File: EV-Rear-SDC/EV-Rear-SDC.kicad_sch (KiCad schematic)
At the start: 74 parts, among them IC2 SCH16T-K01-10, J1 JST-XA, J2 B10B-XASK-1__LF__SN_, J3 Conn_01x14, J4 Conn_01x03, J5 Conn_01x14, J6 JST-XA, K1 Relay_SPDT_G6RN, Q1 BSS205N, Q10 BSS205N, Q11 BSS205N, Q2 BSS205N, Q3 BSS205N, Q4 BSS205N, Q5 BSS205N, Q6 BSS205N, Q7 BSS205N, Q8 BSS205N, Q9 BSS205N, U1 TXE8116DGSR, U2 MAX3390EEUD_T

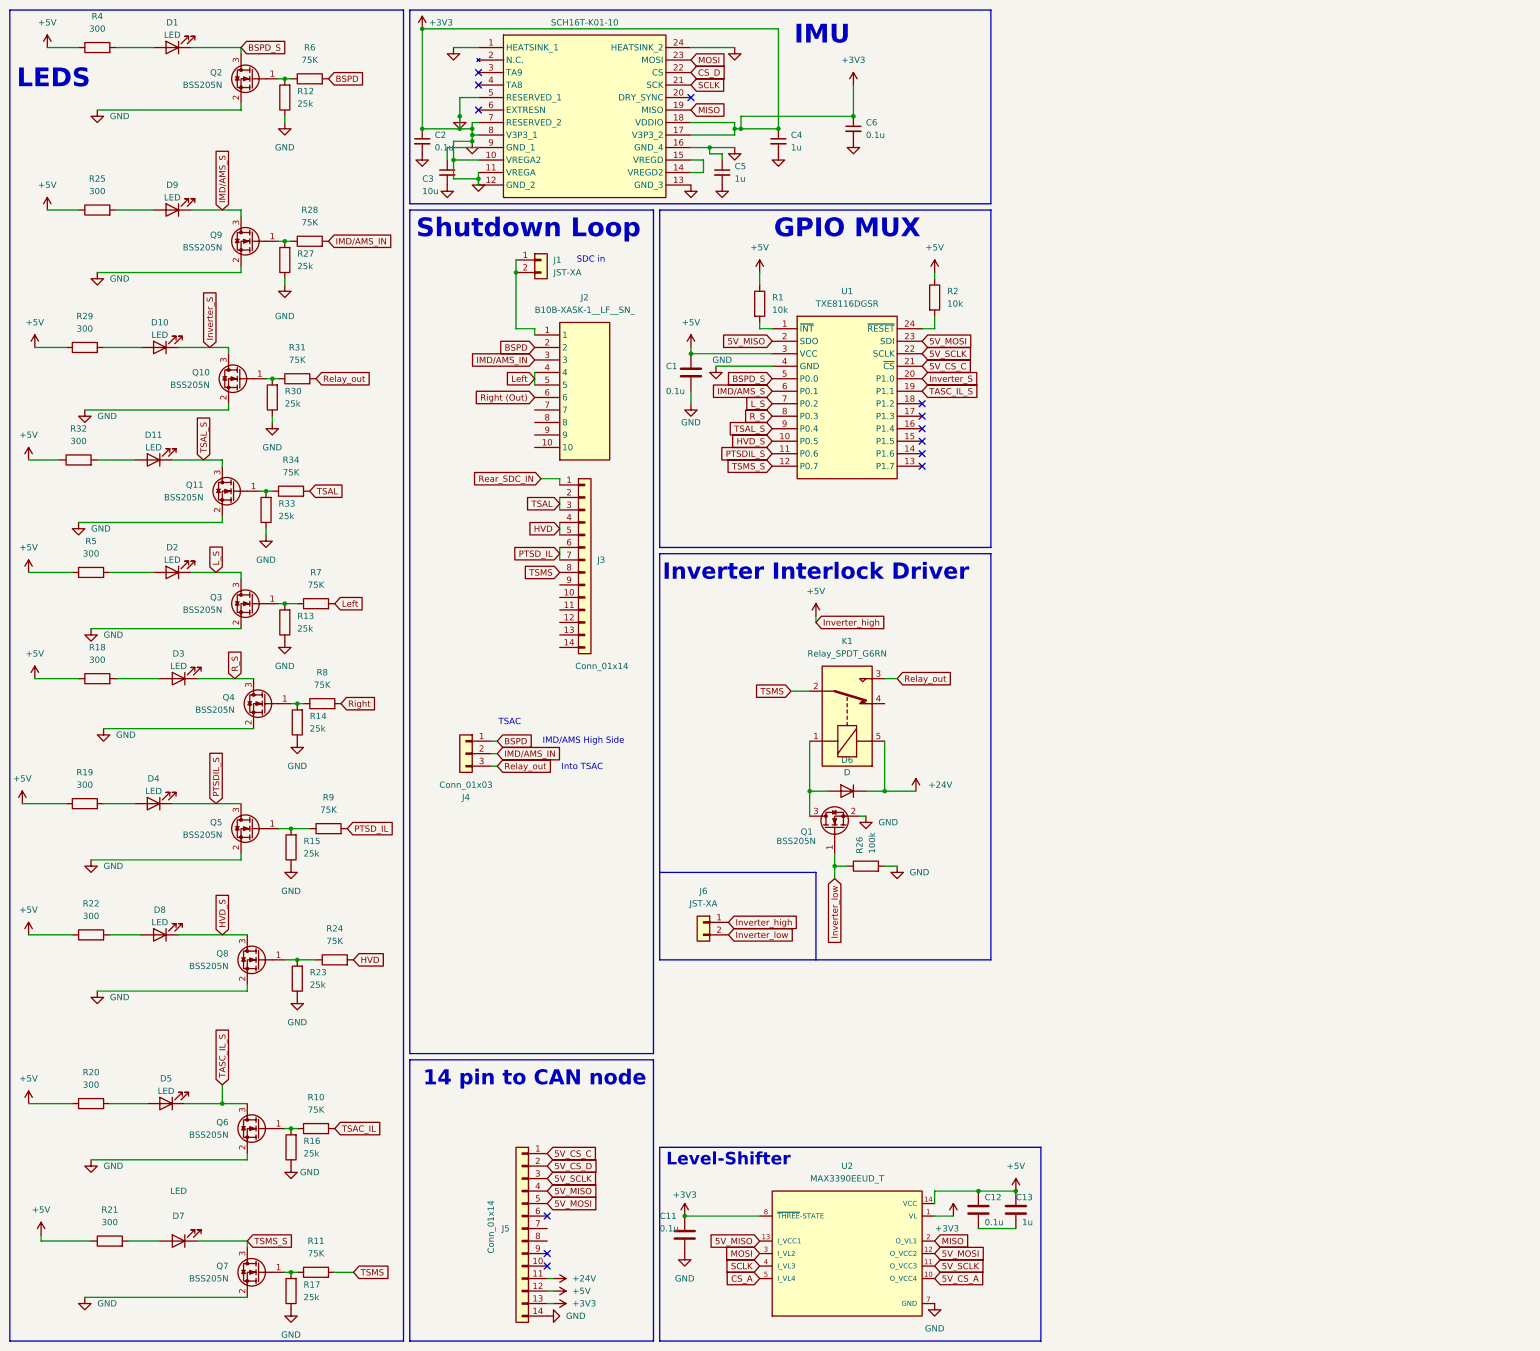
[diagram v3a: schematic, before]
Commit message: Moved Mosfet to avoid EMI error
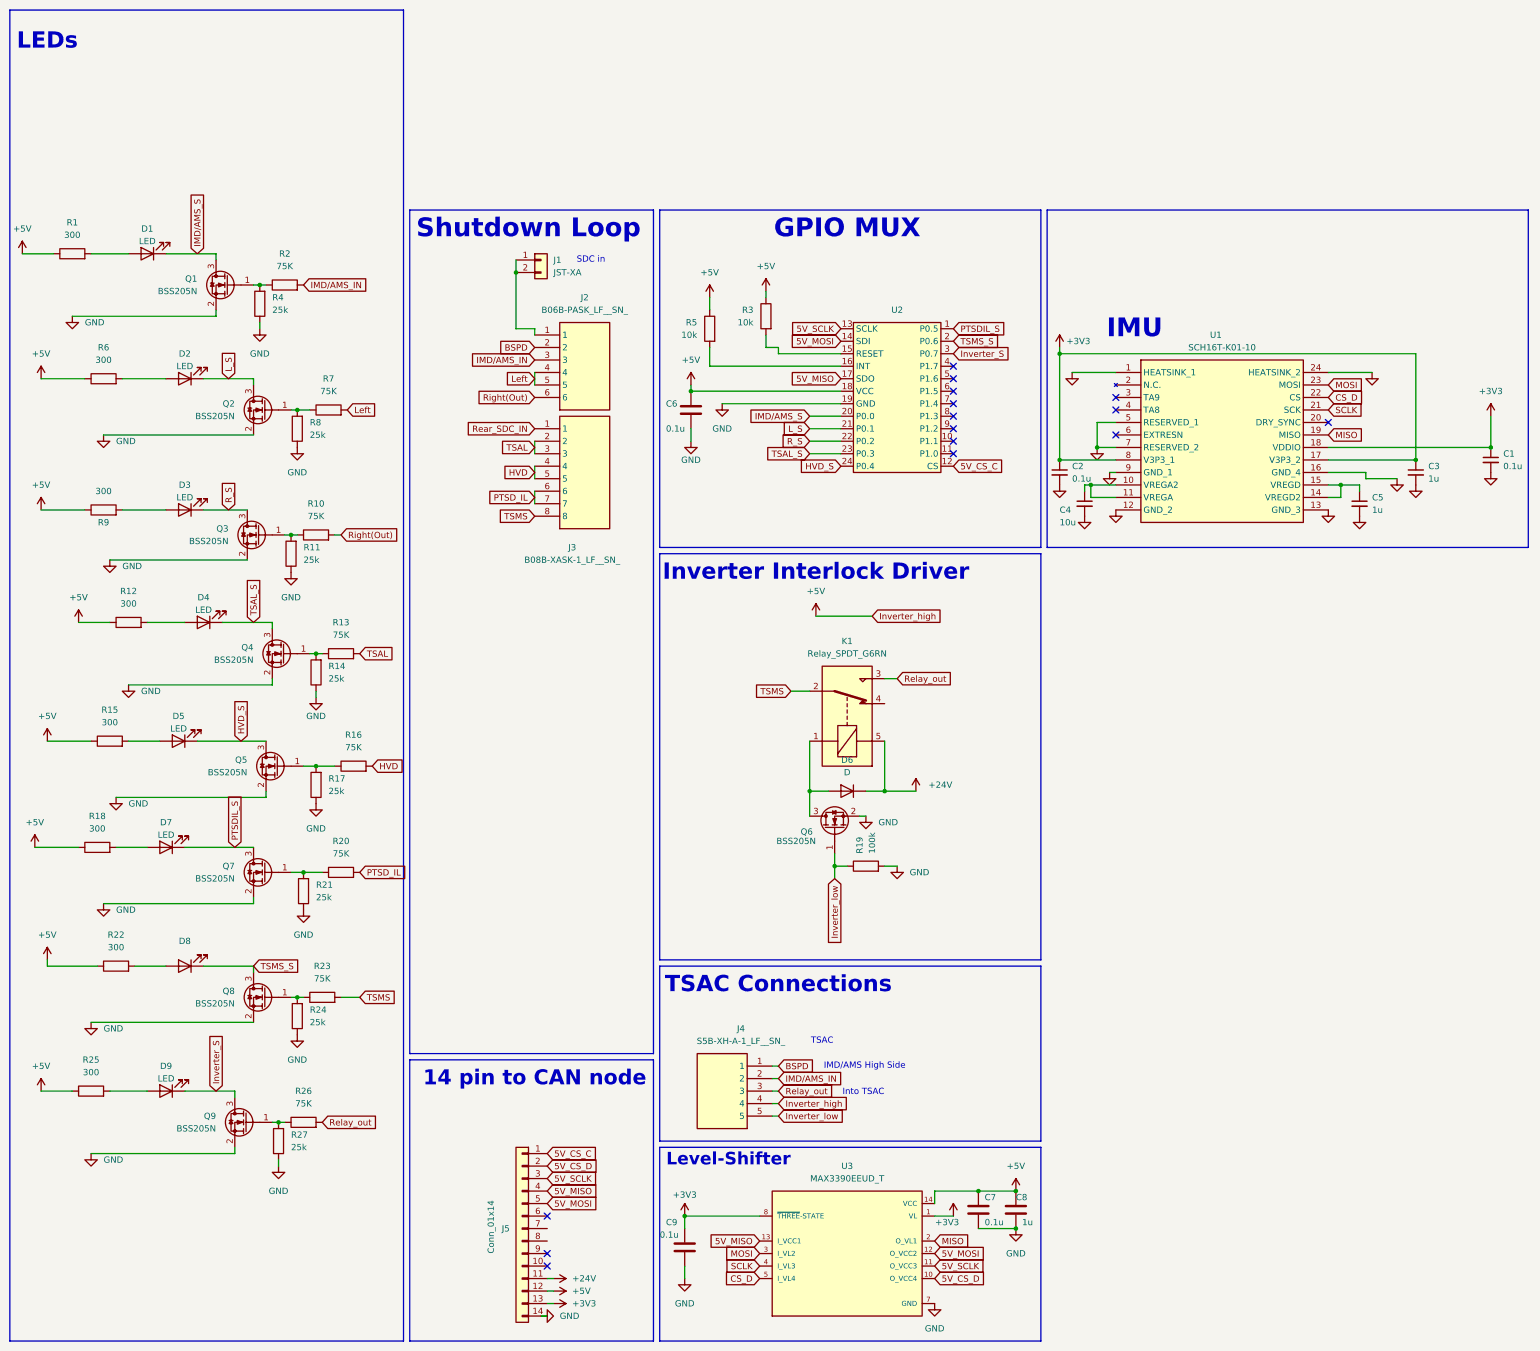
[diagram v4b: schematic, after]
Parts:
- removed C1: 0.1u, Capacitor_SMD:C_0603_1608Metric, symbol Device:C
- removed C6: 0.1u, Capacitor_SMD:C_0603_1608Metric, symbol Device:C_Small
- removed D1, D5: LED, LED_SMD:LED_0603_1608Metric, symbol Device:LED
- removed IC2: SCH16T-K01-10, Custom_MSM:SCH16TK0110, symbol SCH16T-K01-10:SCH16T-K01-10
- removed J2: B10B-XASK-1__LF__SN_, Custom_MSM:B10BXASK1LFSN, symbol B10B-XASK-1__LF__SN_:B10B-XASK-1__LF__SN_
- removed J3: Conn_01x14, Connector_JST:JST_XA_B14B-XASK-1_1x14_P2.50mm_Vertical, symbol Connector_Generic:Conn_01x14
- removed J4: Conn_01x03, Connector_JST:JST_XA_S03B-XASK-1_1x03_P2.50mm_Horizontal, symbol Connector_Generic:Conn_01x03
- removed J6: JST-XA, Custom_MSM:JST_XA_S02B-XASK-1_1x02_P2.50mm_Horizontal, symbol Custom_MSM1:Connector_JST-XA_2POS
- removed Q2, Q6: BSS205N, Custom_MSM:MOSFET_Single_SOT-23, symbol Custom_MSM1:MOSFET_N-CH
- removed R1, R2: 10k, Resistor_SMD:R_0603_1608Metric, symbol Device:R
- removed R10, R6: 75K, Resistor_SMD:R_0603_1608Metric, symbol Device:R
- removed R12, R16: 25k, Resistor_SMD:R_0603_1608Metric, symbol Device:R
- removed R20, R4: 300, Resistor_SMD:R_0603_1608Metric, symbol Device:R
- removed U1: TXE8116DGSR, Custom_MSM:SOP50P490X110-24N, symbol Custom_MSM1:TXE8116DGSR
- added C1: 0.1u, Capacitor_SMD:C_0805_2012Metric, symbol Device:C_Small
- added C6: 0.1u, Capacitor_SMD:C_0805_2012Metric, symbol Device:C
- added J2: B06B-PASK_LF__SN_, Custom_MSM:S06BXASK1LFSN, symbol B06B-PASK_LF__SN_:B06B-PASK_LF__SN_
- added J3: B08B-XASK-1_LF__SN_, Custom_MSM:S08BXASK1LFSN, symbol B08B-XASK-1_LF__SN_:B08B-XASK-1_LF__SN_
- added J4: S5B-XH-A-1_LF__SN_, Custom_MSM:S5BXHA1LFSN, symbol S5B-XH-A-1_LF__SN_:S5B-XH-A-1_LF__SN_
- added R3, R5: 10k, Resistor_SMD:R_0805_2012Metric, symbol Device:R
- added U1: SCH16T-K01-10, Custom_MSM:SCH16TK0110, symbol SCH16T-K01-10:SCH16T-K01-10
- added U2: (no value), Package_DFN_QFN:QFN-24-1EP_4x4mm_P0.5mm_EP2.7x2.7mm, symbol Custom_MSM1:TXE8116RGER
- C2, C5: footprint Capacitor_SMD:C_0603_1608Metric -> Capacitor_SMD:C_0805_2012Metric
- C3: value 10u -> 1u; footprint Capacitor_SMD:C_0603_1608Metric -> Capacitor_SMD:C_0805_2012Metric
- C4: value 1u -> 10u; footprint Capacitor_SMD:C_0603_1608Metric -> Capacitor_SMD:C_0805_2012Metric
- C7: renamed from C12; footprint Capacitor_SMD:C_0603_1608Metric -> Capacitor_SMD:C_0805_2012Metric
- C8: renamed from C13; footprint Capacitor_SMD:C_0603_1608Metric -> Capacitor_SMD:C_0805_2012Metric
- C9: renamed from C11; footprint Capacitor_SMD:C_0603_1608Metric -> Capacitor_SMD:C_0805_2012Metric
- D1: renamed from D9; footprint LED_SMD:LED_0603_1608Metric -> LED_SMD:LED_0805_2012Metric
- D2, D3: footprint LED_SMD:LED_0603_1608Metric -> LED_SMD:LED_0805_2012Metric
- D4: renamed from D11; footprint LED_SMD:LED_0603_1608Metric -> LED_SMD:LED_0805_2012Metric
- D5: renamed from D8; footprint LED_SMD:LED_0603_1608Metric -> LED_SMD:LED_0805_2012Metric
- D6: footprint Diode_SMD:D_0603_1608Metric -> Diode_SMD:D_0805_2012Metric
- D7: renamed from D4; footprint LED_SMD:LED_0603_1608Metric -> LED_SMD:LED_0805_2012Metric
- D8: renamed from D7; footprint LED_SMD:LED_0603_1608Metric -> LED_SMD:LED_0805_2012Metric
- D9: renamed from D10; footprint LED_SMD:LED_0603_1608Metric -> LED_SMD:LED_0805_2012Metric
- R1: renamed from R25; footprint Resistor_SMD:R_0603_1608Metric -> Resistor_SMD:R_0805_2012Metric
- R10: renamed from R8; footprint Resistor_SMD:R_0603_1608Metric -> Resistor_SMD:R_0805_2012Metric
- R11: renamed from R14; footprint Resistor_SMD:R_0603_1608Metric -> Resistor_SMD:R_0805_2012Metric
- R12: renamed from R32; footprint Resistor_SMD:R_0603_1608Metric -> Resistor_SMD:R_0805_2012Metric
- R13: renamed from R34; footprint Resistor_SMD:R_0603_1608Metric -> Resistor_SMD:R_0805_2012Metric
- R14: renamed from R33; footprint Resistor_SMD:R_0603_1608Metric -> Resistor_SMD:R_0805_2012Metric
- R15: renamed from R22; footprint Resistor_SMD:R_0603_1608Metric -> Resistor_SMD:R_0805_2012Metric
- R16: renamed from R24; footprint Resistor_SMD:R_0603_1608Metric -> Resistor_SMD:R_0805_2012Metric
- R17: renamed from R23; footprint Resistor_SMD:R_0603_1608Metric -> Resistor_SMD:R_0805_2012Metric
- R18: renamed from R19; footprint Resistor_SMD:R_0603_1608Metric -> Resistor_SMD:R_0805_2012Metric
- R19: renamed from R26; footprint Resistor_SMD:R_0603_1608Metric -> Resistor_SMD:R_0805_2012Metric
- R2: renamed from R28; footprint Resistor_SMD:R_0603_1608Metric -> Resistor_SMD:R_0805_2012Metric
- R20: renamed from R9; footprint Resistor_SMD:R_0603_1608Metric -> Resistor_SMD:R_0805_2012Metric
- R21: renamed from R15; footprint Resistor_SMD:R_0603_1608Metric -> Resistor_SMD:R_0805_2012Metric
- R22: renamed from R21; footprint Resistor_SMD:R_0603_1608Metric -> Resistor_SMD:R_0805_2012Metric
- R23: renamed from R11; footprint Resistor_SMD:R_0603_1608Metric -> Resistor_SMD:R_0805_2012Metric
- R24: renamed from R17; footprint Resistor_SMD:R_0603_1608Metric -> Resistor_SMD:R_0805_2012Metric
- R25: renamed from R29; footprint Resistor_SMD:R_0603_1608Metric -> Resistor_SMD:R_0805_2012Metric
- R26: renamed from R31; footprint Resistor_SMD:R_0603_1608Metric -> Resistor_SMD:R_0805_2012Metric
- R27: renamed from R30; footprint Resistor_SMD:R_0603_1608Metric -> Resistor_SMD:R_0805_2012Metric
- R4: renamed from R27; footprint Resistor_SMD:R_0603_1608Metric -> Resistor_SMD:R_0805_2012Metric
- R6: renamed from R5; footprint Resistor_SMD:R_0603_1608Metric -> Resistor_SMD:R_0805_2012Metric
- R7: footprint Resistor_SMD:R_0603_1608Metric -> Resistor_SMD:R_0805_2012Metric
- R8: renamed from R13; footprint Resistor_SMD:R_0603_1608Metric -> Resistor_SMD:R_0805_2012Metric
- R9: renamed from R18; footprint Resistor_SMD:R_0603_1608Metric -> Resistor_SMD:R_0805_2012Metric
- U3: renamed from U2; footprint customFootprints:SOP65P640X110-14N -> Custom_MSM:SOP65P640X110-14N
- renumbered Q9 to Q1, Q3 to Q2, Q4 to Q3, Q11 to Q4, Q8 to Q5, Q1 to Q6, Q5 to Q7, Q7 to Q8, Q10 to Q9
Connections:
- net 5V_CS_A is gone; now on net 5V_CS_D: U3.10 (O_VCC4)
- net CS_A is gone; now on net CS_D: U3.5 (I_VL4)
- net +3V3: now also C3.1, C1.1, U1.17 (V3P3_2), U1.18 (VDDIO), U1.8 (V3P3_1); no longer C2.2, C3.2, C4.1, C4.2, C5.1, C5.2, C9.2, J5.14 (Pin_14), Q1.2 (S), Q2.2 (S), Q3.2 (S), Q4.2 (S), Q5.2 (S), Q6.2 (S), Q7.2 (S), Q8.2 (S), Q9.2 (S), R11.1, R14.1, R17.1, R19.2, R21.1, R24.1, R27.1, R4.1, R8.1, U3.7 (GND)
- net +5V: now also C6.1, J4.4, R3.1, R5.1, U2.18 (VCC)
- net 5V_CS_C: now also U2.12 (CS)
- net 5V_MISO: now also U2.17 (SDO)
- net 5V_MOSI: now also U2.14 (SDI)
- net 5V_SCLK: now also U2.13 (SCLK)
- net BSPD: now also J2.2, J4.1
- net CS_D: now also U1.22 (CS)
- net HVD: now also J3.4, J3.5
- net HVD_S: now also U2.24 (P0.4)
- net IMD/AMS_S: now also U2.20 (P0.0)
- net IMD/AMS_IN: now also J2.3, J4.2
- net Inverter_S: now also U2.3 (P0.7)
- net Inverter_low: now also J4.5
- net L_S: now also U2.21 (P0.1)
- net Left: now also J2.4, J2.5
- net MISO: now also U1.19 (MISO)
- net MOSI: now also U1.23 (MOSI)
- net PTSDIL_S: now also U2.1 (P0.5)
- net PTSD_IL: now also J3.6, J3.7
- net R_S: now also U2.22 (P0.2)
- net Rear_SDC_IN: now also J3.1
- net Relay_out: now also J4.3
- net SCLK: now also U1.21 (SCK)
- net TSAL: now also J3.2, J3.3
- net TSAL_S: now also U2.23 (P0.3)
- net TSMS: now also J3.8
- net TSMS_S: now also U2.2 (P0.6)
- net at J1.1 (Pin_1), J1.2 (Pin_2): now also J2.1
- net GND: now reaches C7.2, C8.2
- net GND: now also C2.2, C3.2, C4.2, C5.2, C9.2, J5.14 (Pin_14), Q1.2 (S), Q2.2 (S), Q3.2 (S), Q4.2 (S), Q5.2 (S), Q6.2 (S), Q7.2 (S), Q8.2 (S), Q9.2 (S), R11.1, R14.1, R17.1, R19.2, R21.1, R24.1, R27.1, R4.1, R8.1, U3.7 (GND), C1.2, C6.2, U1.1 (HEATSINK_1), U1.12 (GND_2), U1.13 (GND_3), U1.16 (GND_4), U1.24 (HEATSINK_2), U1.5 (RESERVED_1), U1.7 (RESERVED_2), U1.9 (GND_1), U2.19 (GND)
- net Right renamed Right(Out)
- net Right(Out): now also J2.6
- new net: C4.1, U1.10 (VREGA2), U1.11 (VREGA)
- new net: R5.2, U2.16 (INT)
- new net: R3.2, U2.15 (RESET)
- new net: C5.1, U1.14 (VREGD2), U1.15 (VREGD)
- no-connect marks 13 -> 15
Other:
- note added: "LEDs"
- note added: "TSAC Connections"
- note removed: "LEDS"
- moved on the sheet: C9, D1, D2, D3, D4, D5, D7, D8, D9, Q1, Q2, Q3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

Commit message: Re-routed and did full CC bom for rear
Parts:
- removed J2: B06B-PASK_LF__SN_, Custom_MSM:S06BXASK1LFSN, symbol B06B-PASK_LF__SN_:B06B-PASK_LF__SN_
- removed J3: B08B-XASK-1_LF__SN_, Custom_MSM:S08BXASK1LFSN, symbol B08B-XASK-1_LF__SN_:B08B-XASK-1_LF__SN_
- removed J4: S5B-XH-A-1_LF__SN_, Custom_MSM:S5BXHA1LFSN, symbol S5B-XH-A-1_LF__SN_:S5B-XH-A-1_LF__SN_
- added J2: Conn_01x06, Connector_JST:JST_XA_S06B-XASK-1_1x06_P2.50mm_Horizontal, symbol Connector_Generic:Conn_01x06
- added J3: Conn_01x08, Connector_JST:JST_XA_S08B-XASK-1_1x08_P2.50mm_Horizontal, symbol Connector_Generic:Conn_01x08
- added J4: Conn_01x05, Connector_JST:JST_XA_S05B-XASK-1_1x05_P2.50mm_Horizontal, symbol Connector_Generic:Conn_01x05
- D1, D2, D3, D4, D5, D7, D8, D9: MFN LR Q976.01 -> 150080RS75000; S1PL https://www.mouser.co.uk/en/ProductDetail/ams-OSRAM/LR-Q976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 -> https://www.mouser.co.uk/en/ProductDetail/Wurth-Elektronik/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; S1PN 720-LRQ976.01 -> 710-150080RS75000; S1PRICE (none) -> 0.142; S2PL http://digikey.co.uk/en/products/detail/ams-osram-ag/LR-Q97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 -> https://www.digikey.co.uk/en/products/detail/w%C3%BCrth-ele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; S2PN 475-LRQ976.01-P2R2-1CT-ND -> 732-4984-1-ND; S2PRICE (none) -> 0.140
- D6: MFP (none) -> 1N4148W-E3-08; S1PL (none) -> https://www.mouser.co.uk/en/ProductDetail/Vishay-Semiconduc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; S1PN (none) -> 78-1N4148W-E3-08; S1PRICE (none) -> 0.292; S2PL (none) -> https://www.digikey.co.uk/en/products/detail/vishay-general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; S2PN (none) -> 1N4148W-E3-08TR-ND; S2PRICE (none) -> 0.29
- J1: S1_price (none) -> 0.12; S2_price (none) -> 0.12
- J5: S1PL https://uk.rs-online.com/web/p/pcb-headers/6027837 -> https://www.digikey.co.uk/en/products/detail/jst-sales-amer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; S1PN 602-7837 -> 455-4128-ND; S1_Price (none) -> 0.57; S2PL (none) -> https://www.mouser.co.uk/en/ProductDetail/JST-Commercial/B1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; S2PN (none) -> 306-B14BXASK1LFSN; S2_price (none) -> 0.57
- K1: MFP G6RN-1A DC12 -> G6RN-1A DC24; S1PL https://mou.sr/4hHsX0d -> http://mouser.co.uk/en/ProductDetail/Aratas/G6RN-1A-DC24?qs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; S1PN 653-G6RN-1A-DC12 -> 653-G6RN-1A-DC24; S2PL https://www.digikey.co.uk/short/5w20v31b -> https://www.digikey.co.uk/en/products/detail/aratas-formerl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; S2PN Z988-ND -> Z2347-ND
- Q1, Q2, Q3, Q4, Q5, Q6, Q7, Q8, Q9: S1_price (none) -> 0.32; S2_price (none) -> 0.32
- R1, R12, R15, R18, R22, R25, R6, R9: value 300 -> 300R; MFN CRCW0603300RJNEAHP -> CRCW0805300RFKEA; S1PL https://www.mouser.co.uk/en/ProductDetail/Vishay/CRCW060330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 -> https://www.mouser.co.uk/en/ProductDetail/Vishay/CRCW080530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; S1PN 71-CRCW0603300RJNEAH -> 71-CRCW0805300RFKEA; S1PRICE (none) -> 0.075; S2PL https://www.digikey.co.uk/en/products/detail/vishay-dale/CRCW0603300RJNEAHP/2226560?s=N4IgTCBcDaIMICU4HUAMA2VBmLrUICkA5AUQEEAJABRAF0BfIA -> https://www.digikey.co.uk/en/products/detail/vishay-dale/CRCW0805300RFKEA/1175575; S2PN 541-300SATR-ND -> 541-300CTR-ND; S2PRICE (none) -> 0.07
- R10, R13, R16, R2, R20, R23, R26, R7: MFN TNPW060375K0BHEA -> CRCW080575K0JNEA; S1PN 71-TNPW060375K0BHEA -> 71-CRCW080575K0JNEA; S1PRICE (none) -> 0.075; S2PL https://www.digikey.co.uk/en/products/detail/vishay-dale/tn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 -> https://www.digikey.co.uk/en/products/detail/vishay-dale/CR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; S2PN 541-TNPW060375K0BHEACT-ND -> 541-75KACT-ND; S2PRICE (none) -> 0.07
- R11, R14, R17, R21, R24, R27, R8: MFN PTN0603H2502BST1 -> PNM0805E2502BST1; S1PL https://www.mouser.co.uk/en/ProductDetail/Vishay-Thin-Film/PTN0603H2502BST1?qs=mAH9sUMRCtsUa0oXUVgsJw%3D%3D -> https://www.mouser.co.uk/en/ProductDetail/Vishay-Thin-Film/PNM0805E2502BST1?qs=GmxlWZd7RPJh923cc%252BOgKw%3D%3D; S1PN Images are for reference only See Product Specifications Mo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 -> 71-PNM0805E2502BST1; S1PRICE (none) -> 0.834; S2PL (none) -> https://www.digikey.co.uk/en/products/detail/vishay-dale-th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; S2PN (none) -> 764-PNM0805E2502BST1TR-ND; S2PRICE (none) -> 0.78
- R19: S1PL (none) -> https://www.mouser.co.uk/en/ProductDetail/Vishay/CRCW080510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; S1PN (none) -> 71-CRCW0805100KJNECC; S1_price (none) -> 0.57; S2PL (none) -> https://www.digikey.co.uk/en/products/detail/vishay-dale/CR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; S2PN (none) -> CRCW0805100KJNECC-ND; S2_price (none) -> 0.57
- R3: renamed from R4; MFN PTN0603H2502BST1 -> PNM0805E2502BST1; S1PL https://www.mouser.co.uk/en/ProductDetail/Vishay-Thin-Film/PTN0603H2502BST1?qs=mAH9sUMRCtsUa0oXUVgsJw%3D%3D -> https://www.mouser.co.uk/en/ProductDetail/Vishay-Thin-Film/PNM0805E2502BST1?qs=GmxlWZd7RPJh923cc%252BOgKw%3D%3D; S1PN Images are for reference only See Product Specifications Mo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 -> 71-PNM0805E2502BST1; S1PRICE (none) -> 0.834; S2PL (none) -> https://www.digikey.co.uk/en/products/detail/vishay-dale-th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; S2PN (none) -> 764-PNM0805E2502BST1TR-ND; S2PRICE (none) -> 0.78
- U2: MFP (none) -> TXE8116RGER; S1PL (none) -> https://www.mouser.co.uk/en/ProductDetail/Texas-Instruments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; S1PN (none) -> 595-TXE8116RGER; S1PRICE (none) -> 1.04; S2PL (none) -> https://www.digikey.co.uk/en/products/detail/texas-instrume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; S2PN (none) -> 296-TXE8116RGERTR-ND; S2PRICE (none) -> 1.02
- U3: S1PL (none) -> https://www.mouser.co.uk/en/ProductDetail/Analog-Devices-Ma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; S1PN (none) -> 700-MAX3390EEUDT; S1_price (none) -> 4.69; S2PL (none) -> https://www.digikey.co.uk/en/products/detail/analog-devices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; S2PN (none) -> MAX3390EEUD+TTR-ND; S2_price (none) -> 4.87
- renumbered C6 to C1, C1 to C2, C2 to C3, C3 to C4, C4 to C5, C5 to C6, R3 to R4
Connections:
- net +5V: now also J4.4 (Pin_4)
- net BSPD: now also J2.2 (Pin_2), J4.1 (Pin_1)
- net HVD: now also J3.4 (Pin_4), J3.5 (Pin_5)
- net IMD/AMS_IN: now also J2.3 (Pin_3), J4.2 (Pin_2)
- net Inverter_low: now also J4.5 (Pin_5)
- net Left: now also J2.4 (Pin_4), J2.5 (Pin_5)
- net PTSD_IL: now also J3.6 (Pin_6), J3.7 (Pin_7)
- net Rear_SDC_IN: now also J3.1 (Pin_1)
- net Relay_out: now also J4.3 (Pin_3)
- net Right(Out): now also J2.6 (Pin_6)
- net TSAL: now also J3.2 (Pin_2), J3.3 (Pin_3)
- net TSMS: now also J3.8 (Pin_8)
- net at J1.1 (Pin_1), J1.2 (Pin_2): now also J2.1 (Pin_1)
- no-connect marks 15 -> 17
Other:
- moved on the sheet: J1
